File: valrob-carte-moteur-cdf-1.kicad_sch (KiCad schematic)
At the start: 23 parts, among them J1 Conn_01x04_Pin, J4 USB_C_Receptacle_USB2.0_14P, SW1 SW_Push, SW2 SW_Push, U1 ESP32-S3-WROOM-1, U3 AP2112K-3.3, U7 USBLC6-2SC6

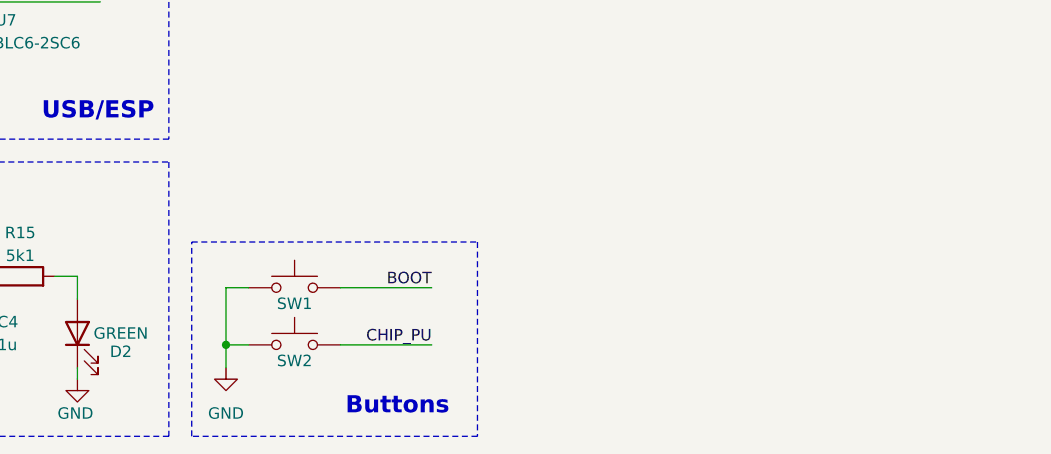
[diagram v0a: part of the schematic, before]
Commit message: schem: add power 5v and 12v power input connectors
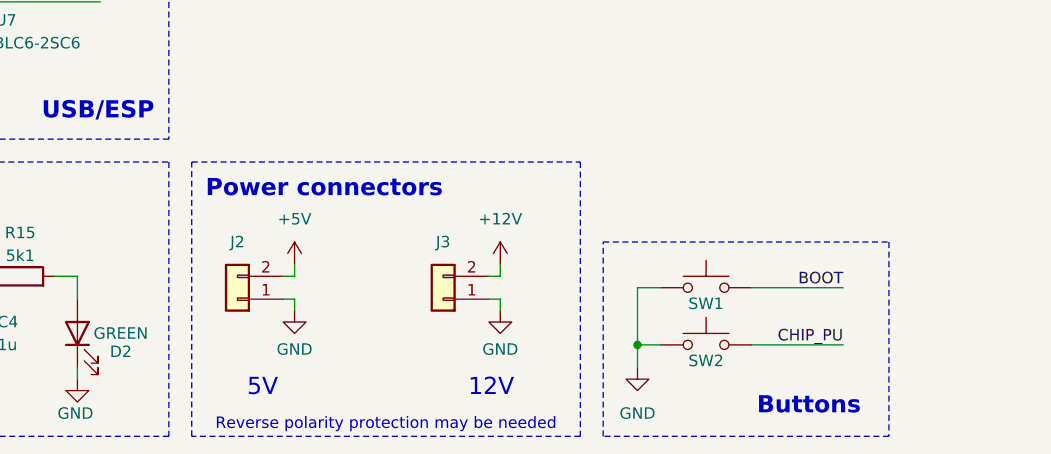
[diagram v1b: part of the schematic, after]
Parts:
- added J2, J3: Conn_01x02, symbol Connector_Generic:Conn_01x02
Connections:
- net +5V: now also J2.2 (Pin_2)
- net GND: now also J2.1 (Pin_1), J3.1 (Pin_1)
- new net +12V: J3.2 (Pin_2)
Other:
- note added: "12V"
- note added: "5V"
- note added: "Power connectors"
- note added: "Reverse polarity protection may be needed"
- moved on the sheet: SW1, SW2

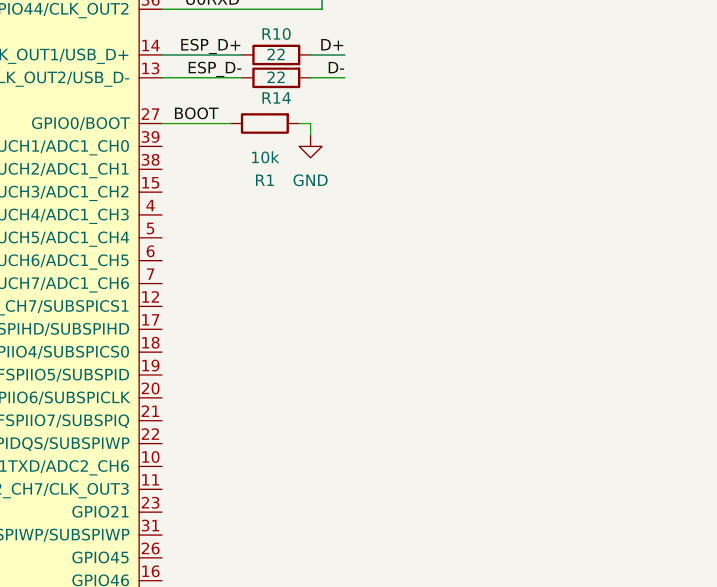
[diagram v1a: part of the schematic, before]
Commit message: schem: add 12v sense from MCU ADC or GPIO
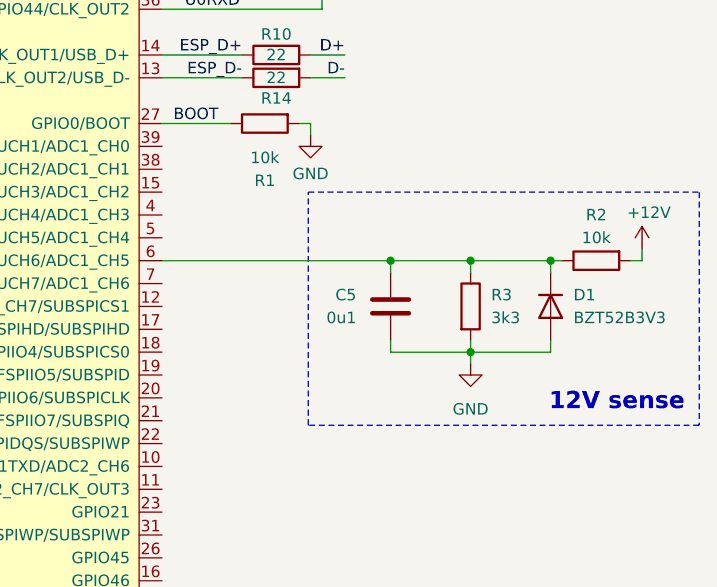
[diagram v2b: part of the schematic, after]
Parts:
- added C5: 0u1, symbol Device:C
- added D1: BZT52B3V3, symbol Device:D
- added R2: 10k, Resistor_SMD:R_0603_1608Metric, symbol Device:R
- added R3: 3k3, symbol Device:R
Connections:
- net +12V: now also R2.2
- net GND: now also C5.2, D1.2 (A), R3.2
- net at U1.6 (GPIO6/TOUCH6/ADC1_CH5): now also C5.1, D1.1 (K), R2.1, R3.1
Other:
- note added: "12V sense"

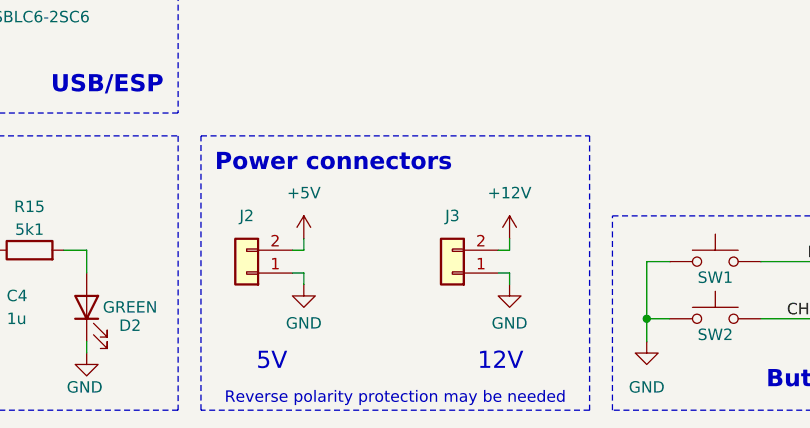
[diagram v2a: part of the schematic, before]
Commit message: schem: add ESD/Surge protection to power inputs
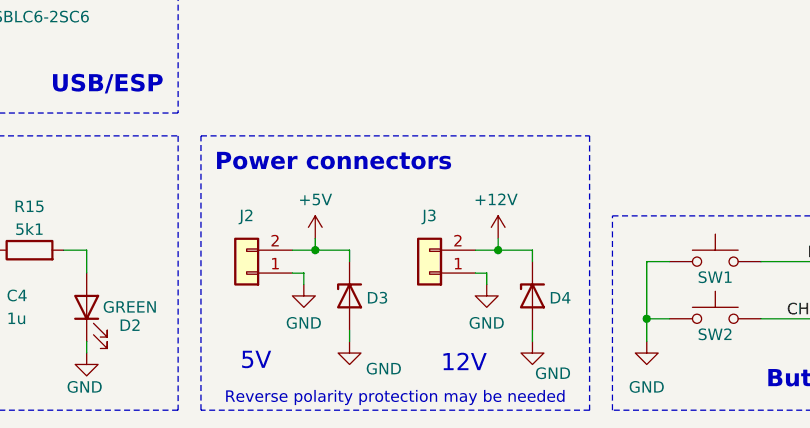
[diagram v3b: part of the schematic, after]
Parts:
- added D3: P6SMB6.8CA/TR13, Diode_SMD:D_SMB, symbol Pers:H5VU10U
- added D4: SMAJ12A, Diode_SMD:D_SMA, symbol Pers:H5VU10U
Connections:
- net +12V: now also D4.1 (K)
- net +5V: now also D3.1 (K)
- net GND: now also D3.2 (A), D4.2 (A)
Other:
- moved on the sheet: J3

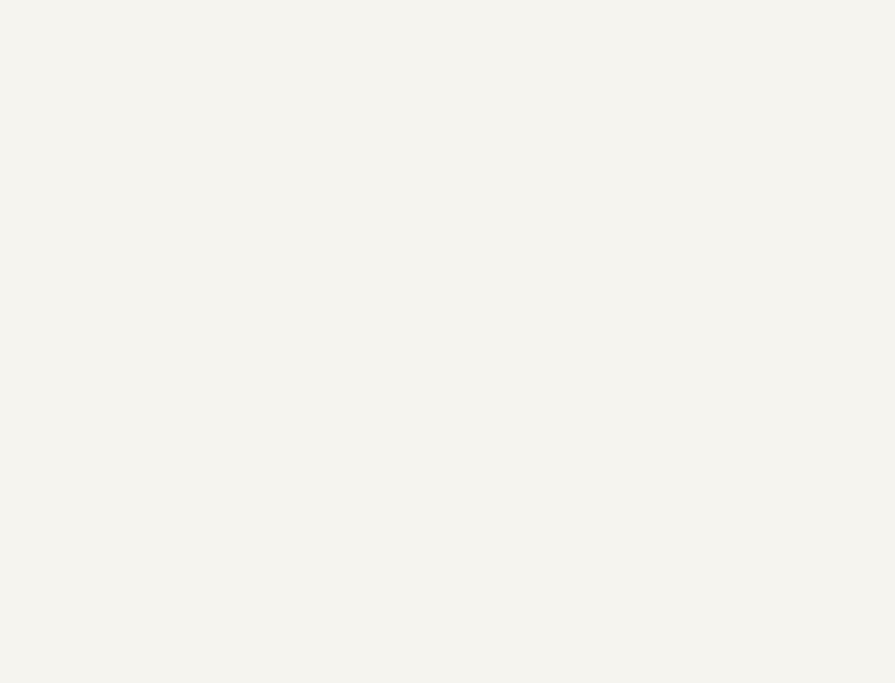
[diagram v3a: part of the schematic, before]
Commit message: schem: add SPI connectors
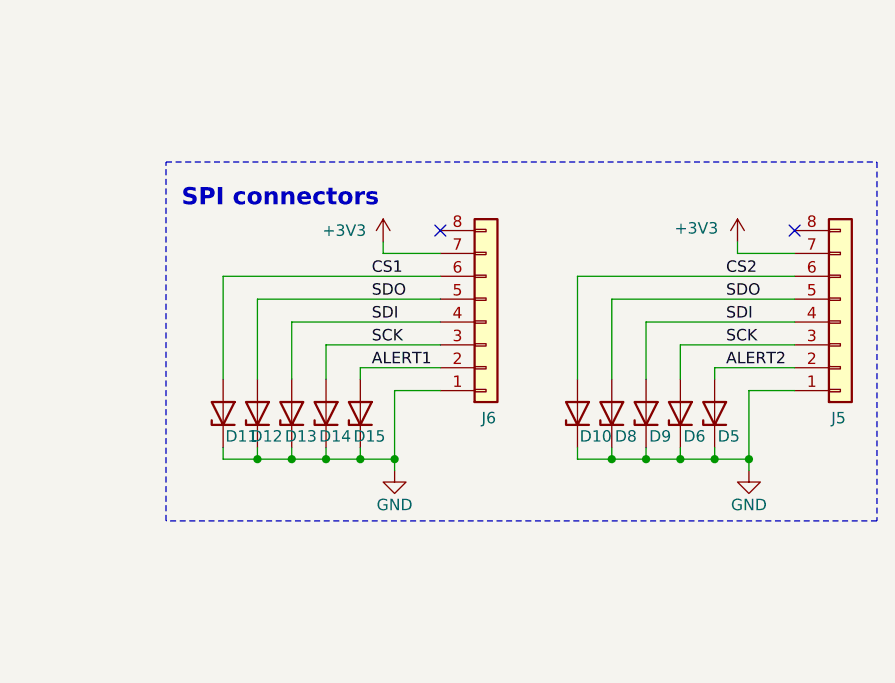
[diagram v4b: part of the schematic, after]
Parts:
- added D10, D11, D12, D13, D14, D15, D5, D6, D8, D9: H5VU10U, Pers:Diode_DFN1006, symbol Pers:H5VU10U
- added J5, J6: Conn_01x08, symbol Connector_Generic:Conn_01x08
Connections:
- net +3V3: now also J5.7 (Pin_7), J6.7 (Pin_7)
- net GND: now also D10.1 (K), D11.1 (K), D12.1 (K), D13.1 (K), D14.1 (K), D15.1 (K), D5.1 (K), D6.1 (K), D8.1 (K), D9.1 (K), J5.1 (Pin_1), J6.1 (Pin_1)
- new net ALERT1: D15.2 (A), J6.2 (Pin_2)
- new net ALERT2: D5.2 (A), J5.2 (Pin_2)
- new net CS1: D11.2 (A), J6.6 (Pin_6)
- new net CS2: D10.2 (A), J5.6 (Pin_6)
- new net SCK: D14.2 (A), D6.2 (A), J5.3 (Pin_3), J6.3 (Pin_3)
- new net SDI: D13.2 (A), D9.2 (A), J5.4 (Pin_4), J6.4 (Pin_4)
- new net SDO: D12.2 (A), D8.2 (A), J5.5 (Pin_5), J6.5 (Pin_5)
- no-connect marks 0 -> 2
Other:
- note added: "SPI connectors"

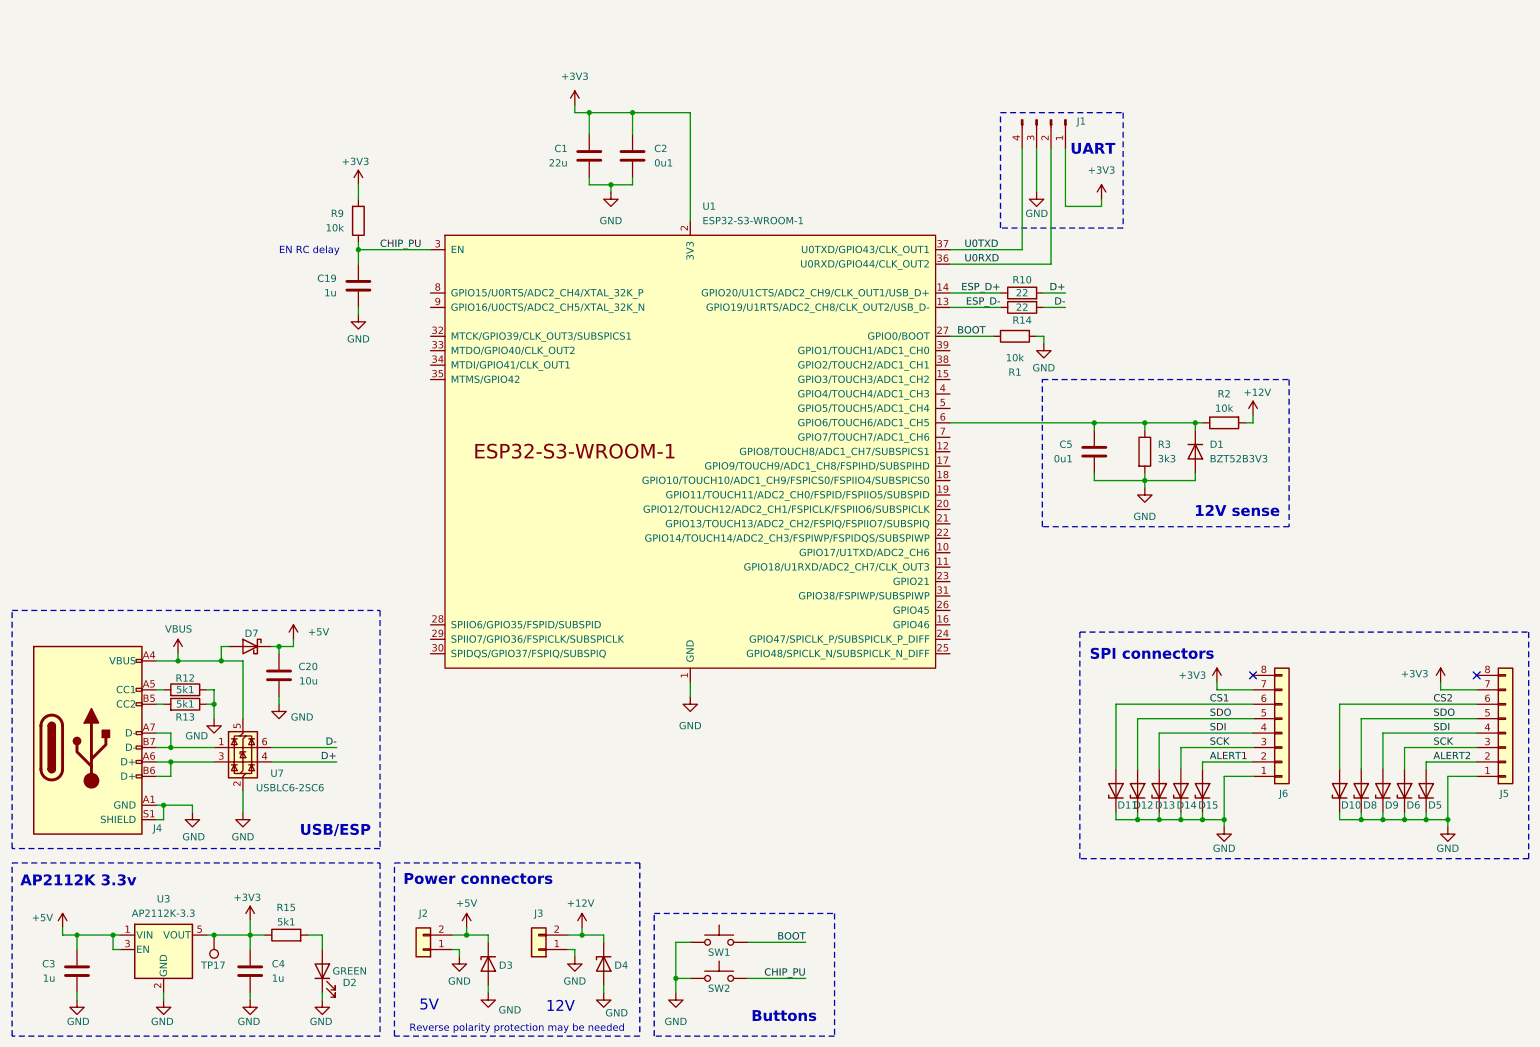
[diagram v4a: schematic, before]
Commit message: schem: add DRV8874 dc motor driver
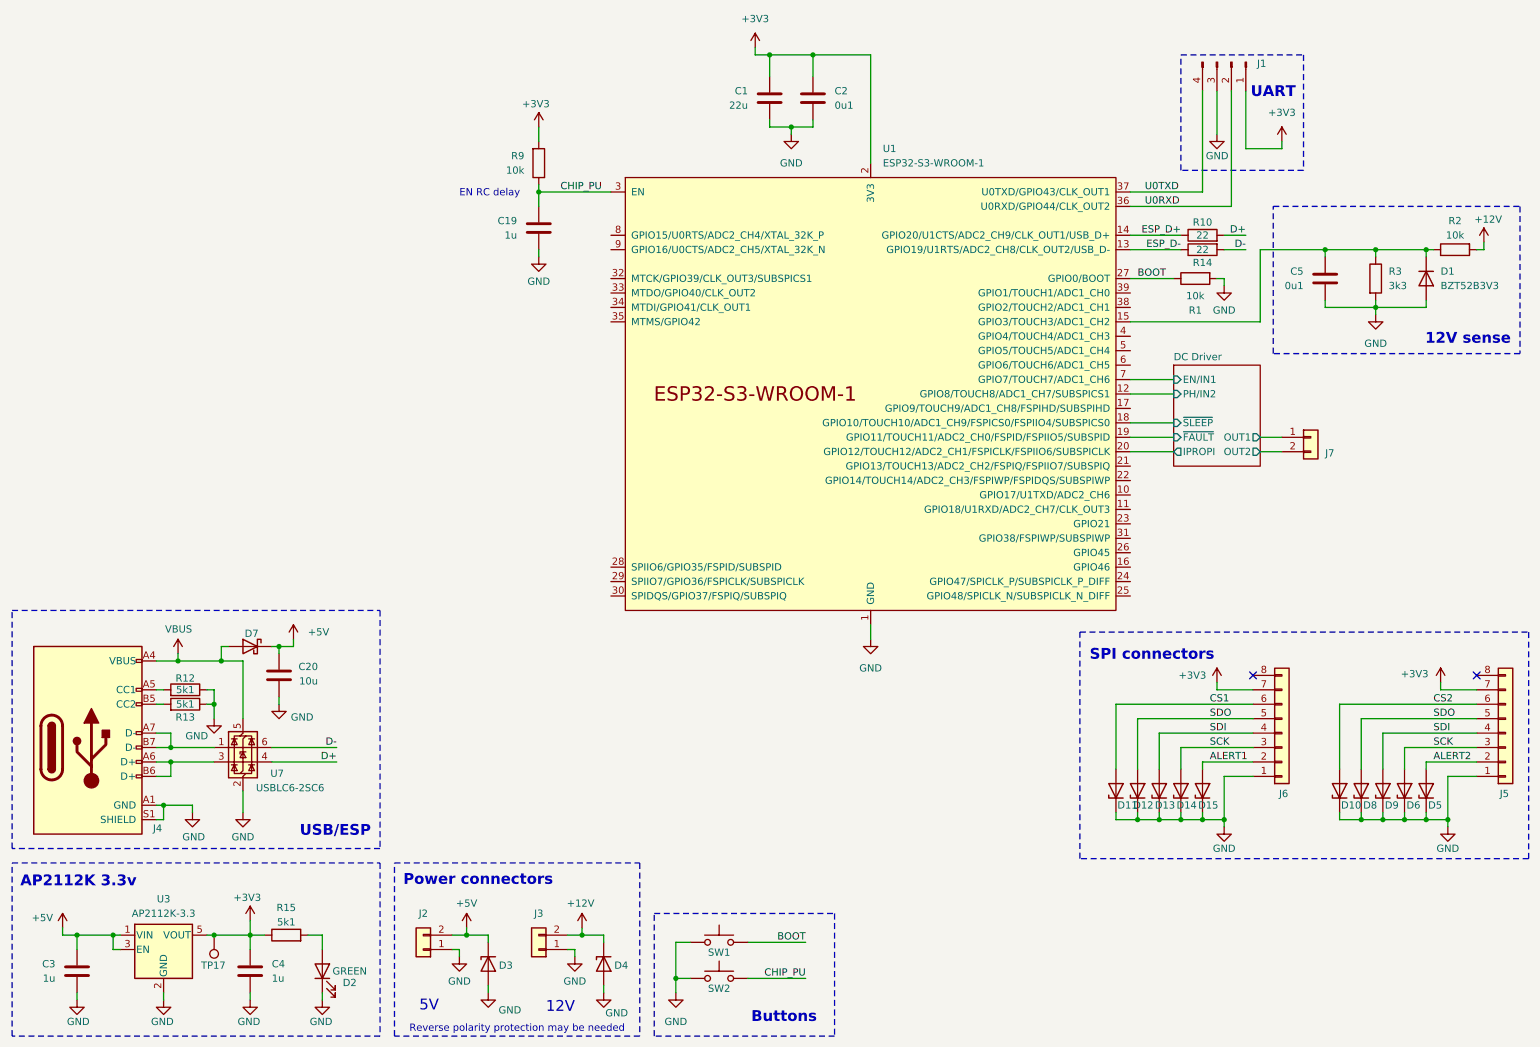
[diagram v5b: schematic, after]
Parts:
- added J7: Conn_01x02, symbol Connector_Generic:Conn_01x02
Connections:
- net at C5.1, D1.1 (K), R2.1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: now also U1.15 (GPIO3/TOUCH3/ADC1_CH2); no longer U1.6 (GPIO6/TOUCH6/ADC1_CH5)
- net DC Driver/PH/IN2: now reaches U1.12 (GPIO8/TOUCH8/ADC1_CH7/SUBSPICS1)
- net DC Driver/~{SLEEP}: now reaches U1.18 (GPIO10/TOUCH10/ADC1_CH9/FSPICS0/FSPIIO4/SUBSPICS0)
- net DC Driver/~{FAULT}: now reaches U1.19 (GPIO11/TOUCH11/ADC2_CH0/FSPID/FSPIIO5/SUBSPID)
- net DC Driver/IPROPI: now reaches U1.20 (GPIO12/TOUCH12/ADC2_CH1/FSPICLK/FSPIIO6/SUBSPICLK)
- net DC Driver/EN/IN1: now reaches U1.7 (GPIO7/TOUCH7/ADC1_CH6)
- new net DC Driver/OUT1: J7.1 (Pin_1)
- new net DC Driver/OUT2: J7.2 (Pin_2)
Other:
- added sheet DC Driver (dc-motor-driver.kicad_sch)
- moved on the sheet: C1, C19, C2, C5, D1, J1, R1, R10, R14, R2, R3, R9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

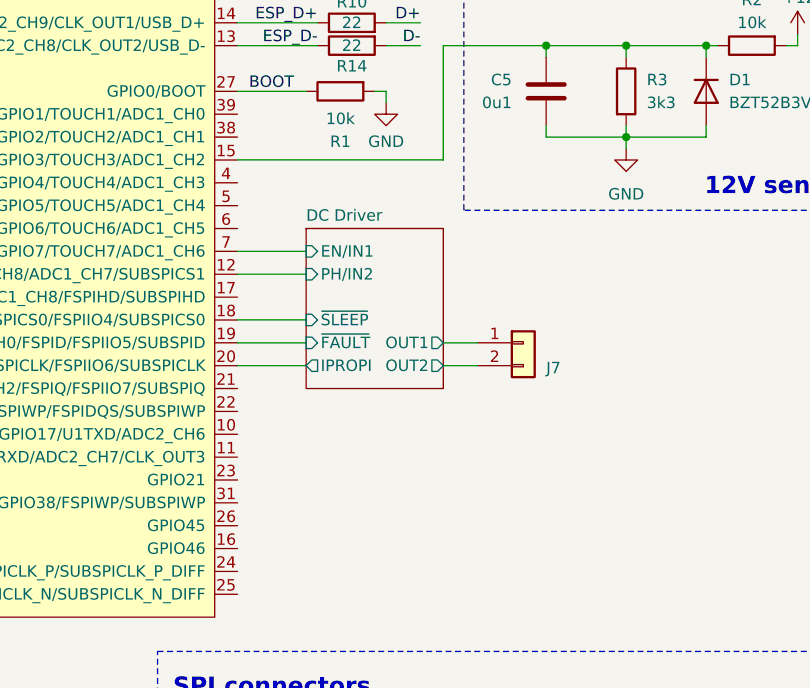
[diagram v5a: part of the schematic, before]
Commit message: schem: add second dc motor driver
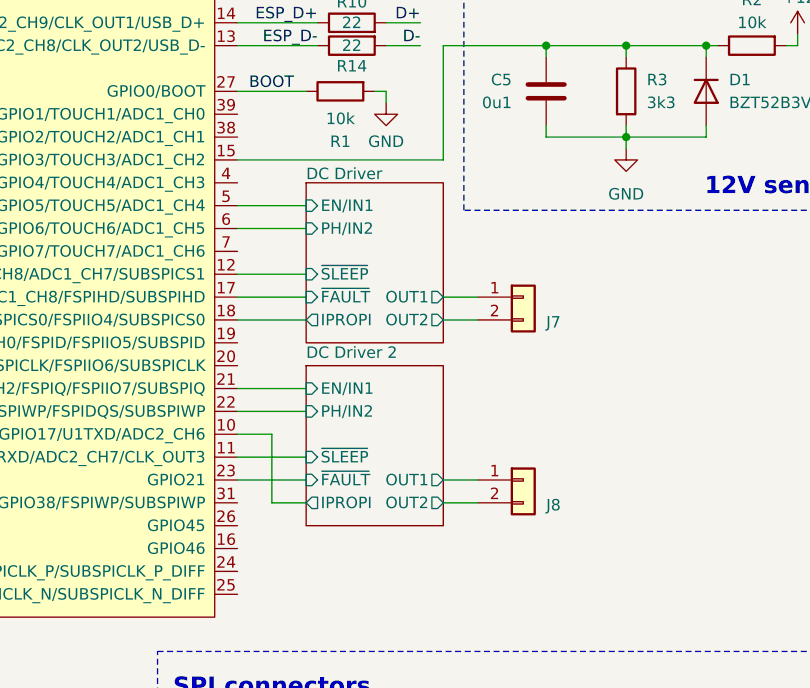
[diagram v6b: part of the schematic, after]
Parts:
- added J8: Conn_01x02, symbol Connector_Generic:Conn_01x02
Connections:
- net DC Driver/EN/IN1: now also U1.5 (GPIO5/TOUCH5/ADC1_CH4); no longer U1.7 (GPIO7/TOUCH7/ADC1_CH6)
- net DC Driver/IPROPI: now also U1.18 (GPIO10/TOUCH10/ADC1_CH9/FSPICS0/FSPIIO4/SUBSPICS0); no longer U1.20 (GPIO12/TOUCH12/ADC2_CH1/FSPICLK/FSPIIO6/SUBSPICLK)
- net DC Driver/PH/IN2: now also U1.6 (GPIO6/TOUCH6/ADC1_CH5); no longer U1.12 (GPIO8/TOUCH8/ADC1_CH7/SUBSPICS1)
- net DC Driver/~{FAULT}: now also U1.17 (GPIO9/TOUCH9/ADC1_CH8/FSPIHD/SUBSPIHD); no longer U1.19 (GPIO11/TOUCH11/ADC2_CH0/FSPID/FSPIIO5/SUBSPID)
- net DC Driver/~{SLEEP}: now also U1.12 (GPIO8/TOUCH8/ADC1_CH7/SUBSPICS1); no longer U1.18 (GPIO10/TOUCH10/ADC1_CH9/FSPICS0/FSPIIO4/SUBSPICS0)
- net DC Driver 2/IPROPI: now reaches U1.10 (GPIO17/U1TXD/ADC2_CH6)
- net DC Driver 2/~{SLEEP}: now reaches U1.11 (GPIO18/U1RXD/ADC2_CH7/CLK_OUT3)
- net DC Driver 2/EN/IN1: now reaches U1.21 (GPIO13/TOUCH13/ADC2_CH2/FSPIQ/FSPIIO7/SUBSPIQ)
- net DC Driver 2/PH/IN2: now reaches U1.22 (GPIO14/TOUCH14/ADC2_CH3/FSPIWP/FSPIDQS/SUBSPIWP)
- net DC Driver 2/~{FAULT}: now reaches U1.23 (GPIO21)
- new net DC Driver 2/OUT1: J8.1 (Pin_1)
- new net DC Driver 2/OUT2: J8.2 (Pin_2)
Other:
- added sheet DC Driver 2 (dc-motor-driver.kicad_sch)
- moved on the sheet: J7
